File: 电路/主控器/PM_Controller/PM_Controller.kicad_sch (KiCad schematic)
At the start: 134 parts, among them J1 Conn_01x04_Socket, J10 Conn_02x04_Odd_Even, J11 Conn_02x06_Odd_Even, J2 Conn_01x04_Socket, J3 Conn_01x04_Socket, J4 Conn_01x04_Socket, J5 Conn_01x02_Pin, J6 Conn_01x02_Pin, J7 Conn_02x04_Odd_Even, J8 Conn_01x04_Pin, J9 Conn_01x04_Socket, P2V5 SolderJumper_2_Open, P3V3 SolderJumper_2_Open, Q1 AO3401A, Q2 AO3400A, Q3 AO3400A, Q4 AO3400A, Q5 AO3400A, Q6 AO3400A, U1 AT24CS08-SSHM, U10 TMP102xxDRL, U11 TPS2552DDBVR, U12 TLP127, U2 AMS1117-3.3, U3 STM32G431RBTx, U4 TPS61085DGK, U5 BQ21040DBV, U6 TPS2552DDBVR, U7 STM32L011D4Px, U8 ME6211C25M5, U9 AT24CS08-SSHM, Y1 32.768kHz, Y2 24Mhz

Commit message: ZUI init
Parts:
- removed C13: 22uf, Capacitor_SMD:C_0603_1608Metric_Pad1.08x0.95mm_HandSolder, symbol Device:C
- removed C15: 100nf, Capacitor_SMD:C_0603_1608Metric_Pad1.08x0.95mm_HandSolder, symbol Device:C
- removed C16: 820pf, Capacitor_SMD:C_0603_1608Metric_Pad1.08x0.95mm_HandSolder, symbol Device:C
- removed C4: 22uf, Capacitor_Tantalum_SMD:CP_EIA-3528-21_Kemet-B_Pad1.50x2.35mm_HandSolder, symbol Device:C_Polarized
- removed C9: 1uf, Capacitor_SMD:C_0603_1608Metric_Pad1.08x0.95mm_HandSolder, symbol Device:C
- removed D1: SS32, Diode_SMD:D_SMA_Handsoldering, symbol Diode:SS32
- removed R10: 82k, Resistor_SMD:R_0603_1608Metric_Pad0.98x0.95mm_HandSolder, symbol Device:R
- removed R11: 27k, Resistor_SMD:R_0603_1608Metric_Pad0.98x0.95mm_HandSolder, symbol Device:R
- removed R9: 56.2k, Resistor_SMD:R_0603_1608Metric_Pad0.98x0.95mm_HandSolder, symbol Device:R
- removed U4: TPS61085DGK, Package_SO:VSSOP-8_3x3mm_P0.65mm, symbol Regulator_Switching:TPS61085DGK
- added C39: 22uf, Capacitor_Tantalum_SMD:CP_EIA-3528-21_Kemet-B_HandSolder, symbol Device:C_Polarized
- added C40: 1uf, Capacitor_SMD:C_1206_3216Metric_Pad1.33x1.80mm_HandSolder, symbol Device:C
- added C41: 10uf, Capacitor_SMD:C_1206_3216Metric_Pad1.33x1.80mm_HandSolder, symbol Device:C
- added D4: 1N5819WS, Diode_SMD:D_SOD-323_HandSoldering, symbol Diode:1N5819WS
- added R43: 150k, Resistor_SMD:R_0603_1608Metric_Pad0.98x0.95mm_HandSolder, symbol Device:R
- added R44: 33k, Resistor_SMD:R_0603_1608Metric_Pad0.98x0.95mm_HandSolder, symbol Device:R
- added R45: 10k, Resistor_SMD:R_0603_1608Metric_Pad0.98x0.95mm_HandSolder, symbol Device:R
- added U13: TLV61048DBVR, SOT-23-6_DBV_TEX, symbol 2025-04-10_12-12-53:TLV61048DBVR
- J5: footprint Connector_Wire:SolderWire-0.1sqmm_1x02_P3.6mm_D0.4mm_OD1mm_Relief -> Connector_Wire:SolderWire-0.5sqmm_1x02_P4.8mm_D0.9mm_OD2.3mm
- L1: footprint Inductor_SMD:L_APV_ANR5040 -> Inductor_SMD:L_APV_APH0650
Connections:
- net BAT_OUT: now also C40.1, R45.2, U13.5 (VIN)
- net GND: now also C39.2, C40.2, C41.2, R44.2, U13.2 (GND)
- net VBAT5: now also C39.1, C41.1, D4.1 (K), R43.1
- net at L1.2: now also D4.2 (A), U13.1 (SW)
- new net: R43.2, R44.1, U13.3 (FB)
- new net: R45.1, U13.4 (EN)
- no-connect marks 11 -> 12

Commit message: 电机软起动加入，效果有限无法防止激光雷达下电
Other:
- title: PM Controller -> PM Controller （最初投产版本）
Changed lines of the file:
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@@
 	(paper "A3")
 	(title_block
-		(title "PM Controller")
+		(title "PM Controller （最初投产版本）")
 		(date "2025-06-13")
 		(rev "1.1")

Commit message: 闪光灯ok
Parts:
- removed P2V5: SolderJumper_2_Open, Jumper:SolderJumper-2_P1.3mm_Open_RoundedPad1.0x1.5mm, symbol Jumper:SolderJumper_2_Open
- added L2, L3: 4.7uH, Inductor_SMD:L_APV_APH0650, symbol Device:L
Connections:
- net +5V: now also L2.1; no longer C17.1, U2.3 (VI)
- net BAT_OUT2: now also L3.2; no longer J9.1 (Pin_1)
- new net: C17.1, L2.2, U2.3 (VI)
- new net: J9.1 (Pin_1), L3.1
- no-connect marks 12 -> 13

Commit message: 优化外壳与5V外部供电电路选择逻辑
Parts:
- removed C12: 47uf, Capacitor_Tantalum_SMD:CP_EIA-3528-21_Kemet-B_Pad1.50x2.35mm_HandSolder, symbol Device:C_Polarized
- removed D2: SS32, Diode_SMD:D_SMA_Handsoldering, symbol Diode:SS32
- removed Q1: AO3401A, Package_TO_SOT_SMD:SOT-23, symbol Transistor_FET:AO3401A
- removed Q4: AO3400A, Package_TO_SOT_SMD:SOT-23, symbol Transistor_FET:AO3400A
- removed R19: 100k, Resistor_SMD:R_0603_1608Metric_Pad0.98x0.95mm_HandSolder, symbol Device:R
- added C12: 22uf, Capacitor_SMD:C_1206_3216Metric_Pad1.33x1.80mm_HandSolder, symbol Device:C
- added C4: 100nf, Capacitor_SMD:C_0603_1608Metric, symbol Device:C
- added D1: SS34, Diode_SMD:D_SMA, symbol Diode:SS34
- added H9: MountingHole_Pad, MountingHole:MountingHole_3.2mm_M3_DIN965_Pad_TopBottom, symbol Mechanical:MountingHole_Pad
- R25, R26, R32, R40, R6: value 100k -> 1k
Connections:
- net EJCMT_GND is gone; now on net GND: J5.2 (Pin_2)
- net VBAT5 is gone; now on net +5V: C39.1, C41.1, D4.1 (K), R43.1
- net +3.3V: now also C12.1
- net +5V: now also D1.1 (K)
- net +5VA: now also D1.2 (A); no longer R6.2
- net +BATT: no longer J5.1 (Pin_1)
- net EJCMT_EN: now also R6.1
- net GND: now also C12.2, C4.2, H9.1; no longer R6.1
- net at R43.2, R44.1, U13.3 (FB): now also C4.1
- new net: J5.1 (Pin_1), R6.2
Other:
- note added: "G474RETx 应该可用"
- note removed: "电路自动切换"
- moved on the sheet: C14, C17, C18, C19, C20, C21, C22, C23, C24, H5, H6, H7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

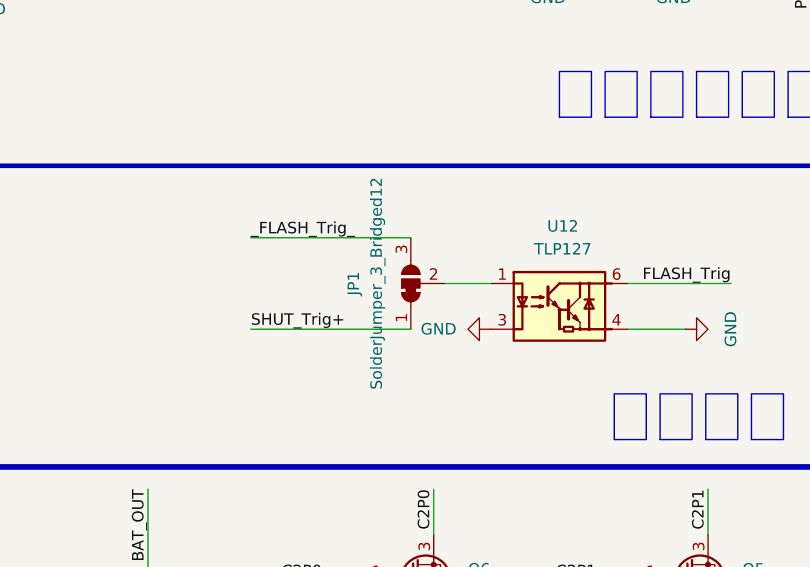
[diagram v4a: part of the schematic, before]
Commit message: 硬件1.3版本，调整闪光灯为默认过MCU
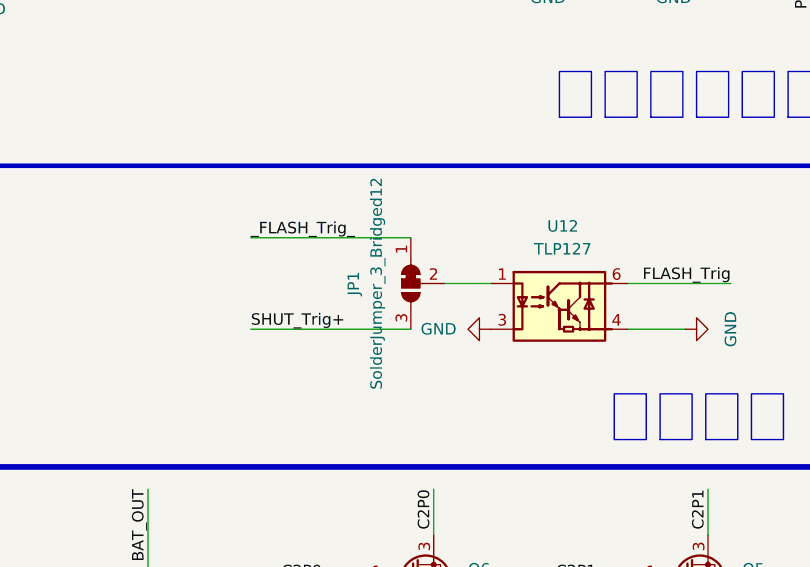
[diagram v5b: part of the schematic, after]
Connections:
- net SHUT_Trig+: now also JP1.3 (B); no longer JP1.1 (A)
- net _FLASH_Trig_: now also JP1.1 (A); no longer JP1.3 (B)
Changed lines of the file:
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@@
 	(title_block
 		(title "PM Controller （最初投产版本）")
-		(date "2026-01-21")
-		(rev "1.2")
+		(date "2026-02-03")
+		(rev "1.3")
 		(company "LiuZS")
-		(comment 1 "20250613-电池升压改为tps61048")
-		(comment 2 "20260121-5V外部电源直供通路取消，电源均通过电池提供")
+		(comment 1 "20250613/1.1-电池升压改为tps61048")
+		(comment 2 "20260121/1.2-5V外部电源直供通路取消，电源均通过电池提供")
+		(comment 3 "20260203/1.3-闪光灯逻辑重新调整，默认过控制器")
 	)
 	(text "温度"
@@
 		(lib_id "Jumper:SolderJumper_3_Bridged12")
 		(at 209.55 160.02 90)
+		(mirror x)
 		(unit 1)
 		(exclude_from_sim yes)
